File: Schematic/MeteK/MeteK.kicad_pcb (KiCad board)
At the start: 2 copper layers, 1 part, among them U2 LM7805_TO220

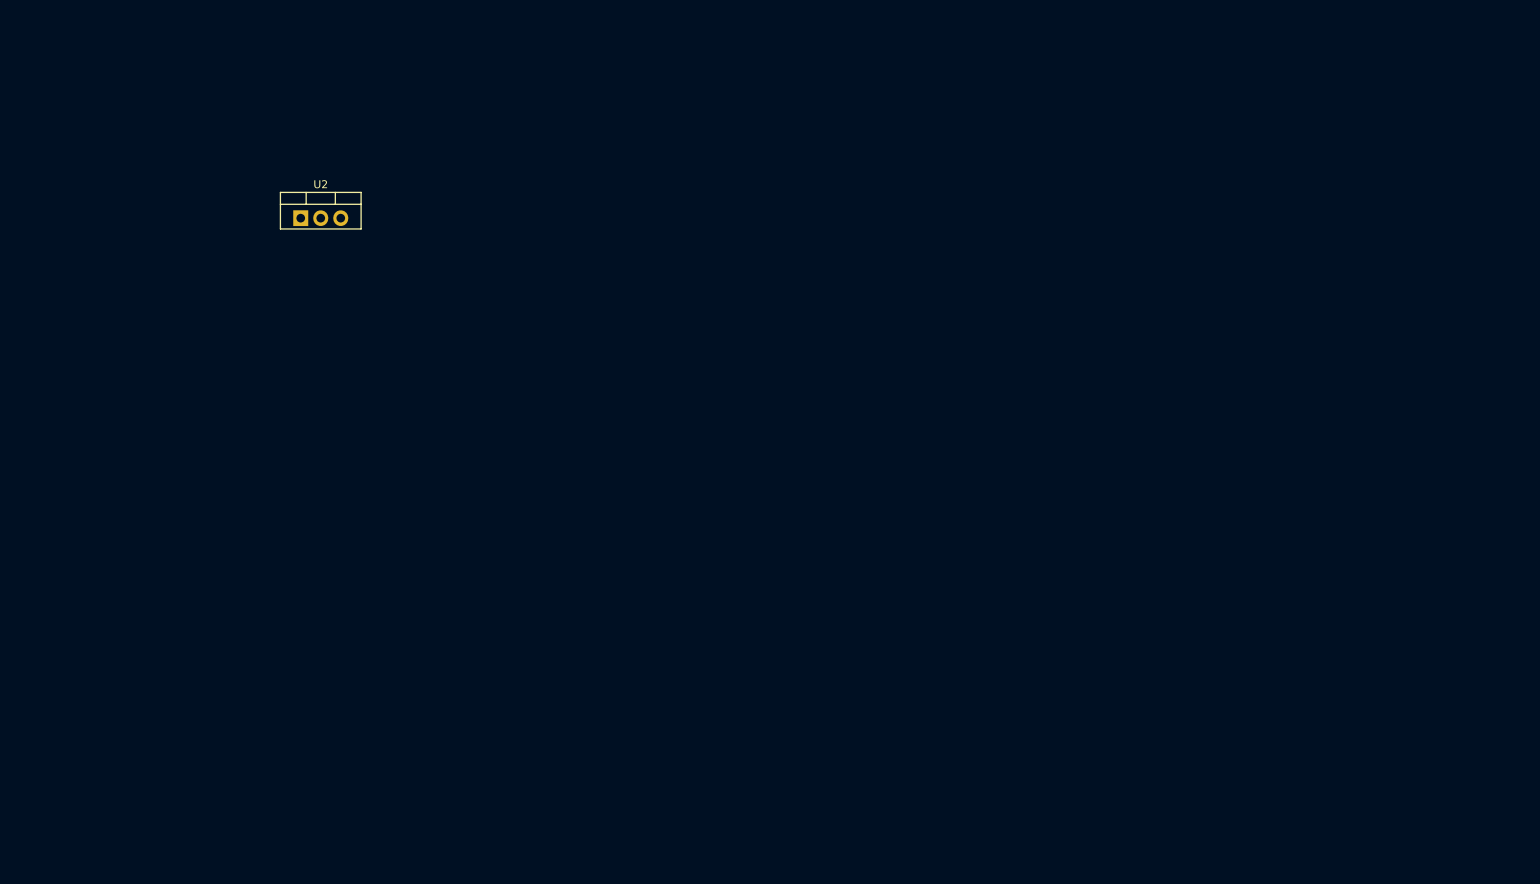
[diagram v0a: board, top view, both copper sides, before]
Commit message: Gate driver fixes. Initial KiCad schematic and PCB design trials. Updates on components.
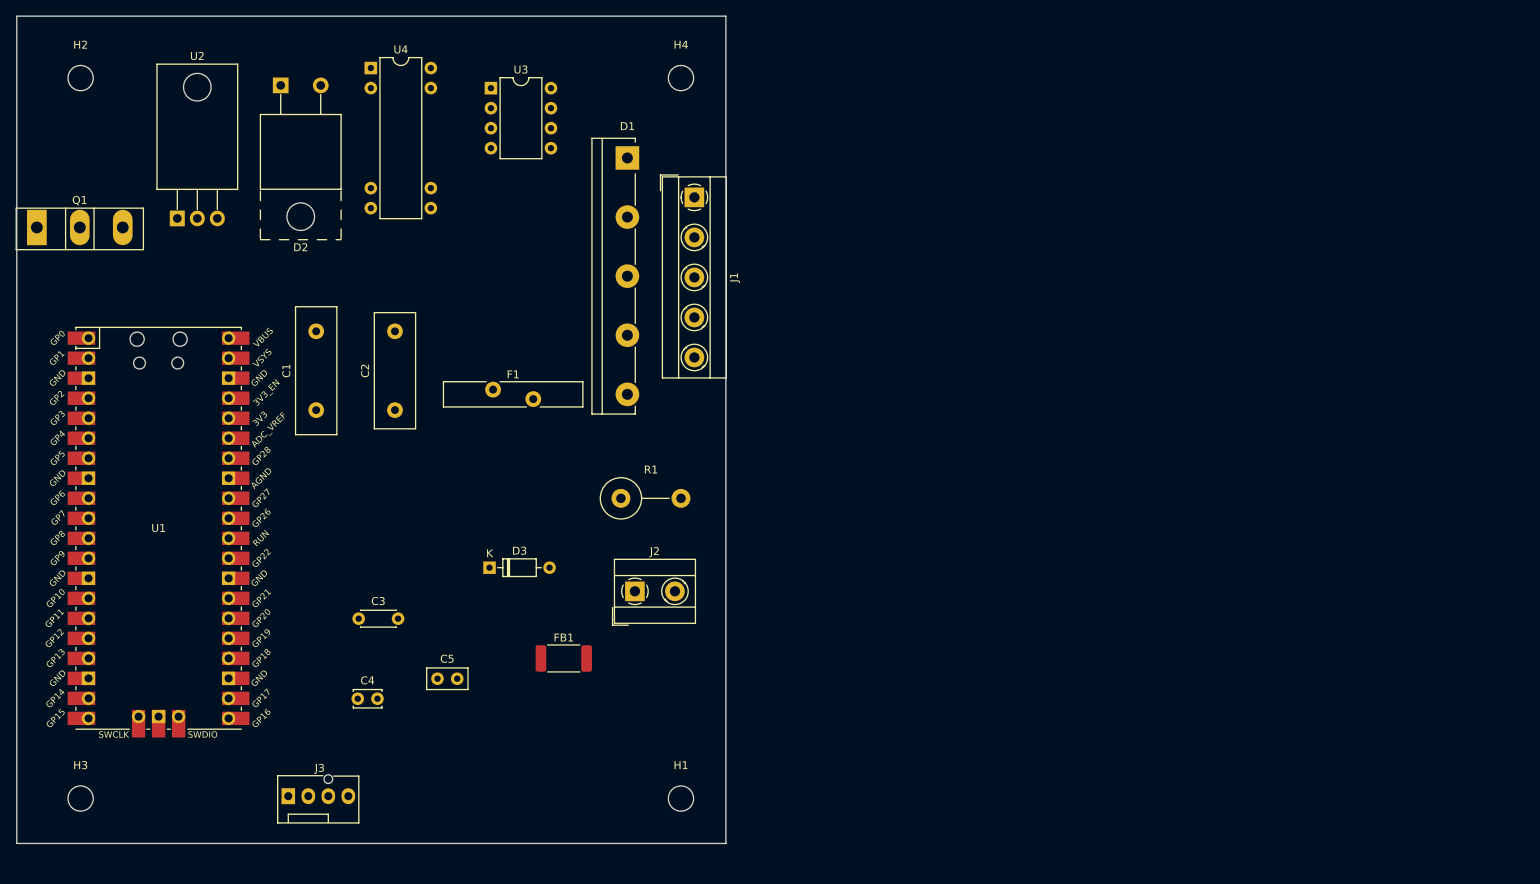
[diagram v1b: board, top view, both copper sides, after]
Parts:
- added C1: 100u, Capacitor_THT:C_Disc_D16.0mm_W5.0mm_P10.00mm, F.Cu at (68.0, 65.0)
- added C2: 0.1u, Capacitor_THT:C_Disc_D14.5mm_W5.0mm_P10.00mm, F.Cu at (78.0, 65.0)
- added C3: 0.1u, Capacitor_THT:C_Disc_D4.3mm_W1.9mm_P5.00mm, F.Cu at (73.4, 91.5)
- added C4: 0.33u, Capacitor_THT:C_Disc_D3.4mm_W2.1mm_P2.50mm, F.Cu at (73.3, 101.6)
- added C5: 0.1u, Capacitor_THT:C_Disc_D5.0mm_W2.5mm_P2.50mm, F.Cu at (83.4, 99.1)
- added D1: GUO40-12NO1, Diode_THT:Diode_Bridge_IXYS_GUFP, F.Cu at (107.5, 33.0)
- added D2: DIODE, Package_TO_SOT_THT:TO-220-2_Horizontal_TabUp, F.Cu at (63.5, 23.8)
- added D3: 1N4148, Diode_THT:D_DO-35_SOD27_P7.62mm_Horizontal, F.Cu at (90.0, 85.0)
- added F1: Fuse, Fuse:Fuse_Bourns_MF-RG1100, F.Cu at (90.5, 62.4)
- added FB1: FerriteBead_Small, Inductor_SMD:L_2512_6332Metric, F.Cu at (99.4, 96.5)
- added H1: MountingHole, MountingHole:MountingHole_3.2mm_M3, F.Cu at (114.3, 114.3)
- added H2: MountingHole, MountingHole:MountingHole_3.2mm_M3, F.Cu at (38.1, 22.9)
- added H3: MountingHole, MountingHole:MountingHole_3.2mm_M3, F.Cu at (38.1, 114.3)
- added H4: MountingHole, MountingHole:MountingHole_3.2mm_M3, F.Cu at (114.3, 22.9)
- added J1: Screw_Terminal_01x05, TerminalBlock_MetzConnect:TerminalBlock_MetzConnect_Type101_RT01605HBWC_1x05_P5.08mm_Horizontal, F.Cu at (116.0, 38.0)
- added J2: Screw_Terminal_01x02, TerminalBlock_MetzConnect:TerminalBlock_MetzConnect_Type101_RT01602HBWC_1x02_P5.08mm_Horizontal, F.Cu at (108.5, 88.0)
- added J3: Conn_01x04_Female, Connector:FanPinHeader_1x04_P2.54mm_Vertical, F.Cu at (64.5, 114.0)
- added Q1: IRG4PF50W, Package_TO_SOT_THT:TO-247-3_Vertical, F.Cu at (32.5, 41.8)
- added R1: R, Resistor_THT:R_Axial_DIN0516_L15.5mm_D5.0mm_P7.62mm_Vertical, F.Cu at (106.7, 76.2)
- added U1: Pico, MCU_RaspberryPi_and_Boards:RPi_Pico_SMD_TH, F.Cu at (48.0, 80.0)
- added U3: HCPL-3120, Package_DIP:DIP-8_W7.62mm, F.Cu at (90.2, 24.1)
- added U4: LM358, Package_DIP:DIP-8-16_W7.62mm, F.Cu at (74.9, 21.6)
- U2: footprint Package_TO_SOT_THT:TO-220-3_Vertical -> Package_TO_SOT_THT:TO-220-3_Horizontal_TabDown
- moved U2 15.7 mm to (50.4, 40.7)
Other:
- board outline added: 90 x 105 mm

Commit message: further tests on schematic and pcb layout.
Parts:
- removed FB1: FerriteBead_Small, Inductor_SMD:L_2512_6332Metric
- added C10: 0.33uF, Capacitor_SMD:C_1206_3216Metric, F.Cu at (200.5, 117.1)
- added C11: 0.1uF, Capacitor_SMD:C_1206_3216Metric, F.Cu at (200.5, 114.1)
- added C12: 0.1uF, Capacitor_SMD:C_1206_3216Metric, F.Cu at (193.0, 79.9)
- added C13: 0.01uF, Capacitor_SMD:C_1206_3216Metric, F.Cu at (204.6, 83.7)
- added C6: 470u, Capacitor_THT:CP_Radial_D35.0mm_P10.00mm_SnapIn, B.Cu at (134.8, 89.8)
- added C7: 470u, Capacitor_THT:CP_Radial_D35.0mm_P10.00mm_SnapIn, B.Cu at (137.8, 54.2)
- added C8: 0.01uF, Capacitor_SMD:C_1206_3216Metric, F.Cu at (151.2, 111.5)
- added C9: 0.1uF, Capacitor_SMD:C_1206_3216Metric, F.Cu at (147.4, 111.5)
- added J4: Conn_01x03_Female, Connector_PinHeader_2.54mm:PinHeader_1x03_P2.54mm_Vertical, F.Cu at (198.2, 80.5)
- added L1: 27n, Inductor_SMD:L_1206_3216Metric, F.Cu at (175.2, 80.2)
- added R2: 220R, Resistor_SMD:R_0805_2012Metric, F.Cu at (156.0, 101.0)
- added R3: 220R, Resistor_SMD:R_0805_2012Metric, F.Cu at (156.0, 97.5)
- added R4: 22R, Resistor_SMD:R_0805_2012Metric, F.Cu at (162.2, 101.0)
- added R5: 22kR, Resistor_SMD:R_0805_2012Metric, F.Cu at (203.4, 77.1)
- added R6: 39kR, Resistor_SMD:R_0805_2012Metric, F.Cu at (206.5, 77.1)
- added R7: 440, Resistor_SMD:R_0805_2012Metric, F.Cu at (189.9, 84.5)
- added U5: L78L12_SOT89, Package_TO_SOT_SMD:SOT-89-3, F.Cu at (207.2, 115.6)
- added U6: LM358, Package_DIP:DIP-8_W7.62mm, F.Cu at (209.4, 76.1)
- C1: value 100u -> 1uF; footprint Capacitor_THT:C_Disc_D16.0mm_W5.0mm_P10.00mm -> Capacitor_SMD:C_1206_3216Metric
- C2: value 0.1u -> 0.1uF; footprint Capacitor_THT:C_Disc_D14.5mm_W5.0mm_P10.00mm -> Capacitor_SMD:C_1206_3216Metric
- C3: value 0.1u -> 0.33uF; footprint Capacitor_THT:C_Disc_D4.3mm_W1.9mm_P5.00mm -> Capacitor_SMD:C_1206_3216Metric
- C4: value 0.33u -> 0.33uF; footprint Capacitor_THT:C_Disc_D3.4mm_W2.1mm_P2.50mm -> Capacitor_SMD:C_1206_3216Metric
- C5: value 0.1u -> 0.1uF; footprint Capacitor_THT:C_Disc_D5.0mm_W2.5mm_P2.50mm -> Capacitor_SMD:C_1206_3216Metric
- D2: footprint Package_TO_SOT_THT:TO-220-2_Horizontal_TabUp -> Package_TO_SOT_THT:TO-220-2_Vertical
- D3: footprint Diode_THT:D_DO-35_SOD27_P7.62mm_Horizontal -> Diode_SMD:D_SMB
- F1: footprint Fuse:Fuse_Bourns_MF-RG1100 -> Fuse:Fuseholder_Clip-5x20mm_Bel_FC-203-22_Lateral_P17.80x5.00mm_D1.17mm_Horizontal
- H1, H2, H3, H4: footprint MountingHole:MountingHole_3.2mm_M3 -> MountingHole:MountingHole_3.2mm_M3_Pad
- J3: value Conn_01x04_Female -> Conn_01x02_Female; footprint Connector:FanPinHeader_1x04_P2.54mm_Vertical -> Connector_PinHeader_2.54mm:PinHeader_1x02_P2.54mm_Vertical
- R1: value R -> 220; footprint Resistor_THT:R_Axial_DIN0516_L15.5mm_D5.0mm_P7.62mm_Vertical -> Resistor_SMD:R_0603_1608Metric
- U2: value LM7805_TO220 -> L78L33_SOT89; footprint Package_TO_SOT_THT:TO-220-3_Horizontal_TabDown -> Package_TO_SOT_SMD:SOT-89-3
- U4: value LM358 -> L78L05_SOT89; footprint Package_DIP:DIP-8-16_W7.62mm -> Package_TO_SOT_SMD:SOT-89-3
- moved Q1 151.2 mm to (181.5, 68.0), turned to 90 degrees
- moved U1 145.7 mm to (192.5, 99.0), turned to 90 degrees
- moved J3 130.3 mm to (194.7, 116.6), turned to 180 degrees
- moved H2 128.7 mm to (122.5, 120.0)
- moved U4 125.1 mm to (187.1, 76.9), turned to 180 degrees
- moved C3 120.8 mm to (193.1, 75.4)
- moved U2 119.9 mm to (163.5, 80.4), turned to 180 degrees
- moved U3 115.8 mm to (163.5, 113.8), turned to 180 degrees
- moved H3 114.1 mm to (122.5, 37.5)
- moved C1 114.0 mm to (180.3, 84.6), turned to 0 degrees
- moved D2 106.6 mm to (162.8, 62.5), turned to -90 degrees
- moved F1 105.0 mm to (193.7, 43.1), turned to 180 degrees
- moved H4 104.2 mm to (217.5, 37.5)
- moved H1 103.4 mm to (217.5, 120.0)
- moved C2 101.7 mm to (178.5, 80.3)
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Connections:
- net +5VA renamed +3.3VA
- C3 pad 1: +5V -> VCC
- C5 pad 1: +5V -> +3.3V
- D1 pad 1: unconnected-(D1-Pad1) -> Net-(D1-Pad1)
- D1 pad 2: unconnected-(D1-Pad2) -> AC_c
- D1 pad 3: unconnected-(D1-Pad3) -> AC_b
- D1 pad 4: unconnected-(D1-Pad4) -> AC_a
- D1 pad 5: unconnected-(D1-Pad5) -> REC_-
- D2 pad 1: unconnected-(D2-Pad1) -> A-
- D2 pad 2: unconnected-(D2-Pad2) -> A+
- D3 pad 1: unconnected-(D3-Pad1) -> Net-(D3-Pad1)
- D3 pad 2: unconnected-(D3-Pad2) -> Net-(D3-Pad2)
- F1 pad 1: unconnected-(F1-Pad1) -> Net-(D1-Pad1)
- F1 pad 2: unconnected-(F1-Pad2) -> A+
- J1 pad 1: unconnected-(J1-Pad1) -> AC_c
- J1 pad 2: unconnected-(J1-Pad2) -> AC_b
- J1 pad 3: unconnected-(J1-Pad3) -> AC_a
- J1 pad 4: unconnected-(J1-Pad4) -> VCC
- J1 pad 5: unconnected-(J1-Pad5) -> GND
- J2 pad 1: unconnected-(J2-Pad1) -> A-
- J2 pad 2: unconnected-(J2-Pad2) -> A+
- J3 pad 1: unconnected-(J3-Pad1) -> GND
- J3 pad 2: unconnected-(J3-Pad2) -> +12V
- Q1 pad 1: unconnected-(Q1-Pad1) -> GATE
- Q1 pad 2: unconnected-(Q1-Pad2) -> A-
- Q1 pad 3: unconnected-(Q1-Pad3) -> REC_-
- R1 pad 1: unconnected-(R1-Pad1) -> PWM
- R1 pad 2: unconnected-(R1-Pad2) -> Net-(R1-Pad2)
- U1 pad 1: unconnected-(U1-Pad1) -> PWM
- U1 pad 19: PWM -> unconnected-(U1-Pad19)
- U1 pad 31: unconnected-(U1-Pad31) -> Net-(U1-Pad31)
- U1 pad 39: +5V -> +3.3V
- U1 pad 40: +5V -> unconnected-(U1-Pad40)
- U2 pad 1: VCC -> +3.3V
- U2 pad 3: +5V -> VCC
- U3 pad 2: unconnected-(U3-Pad2) -> Net-(R1-Pad2)
- U3 pad 3: unconnected-(U3-Pad3) -> GND
- U3 pad 5: unconnected-(U3-Pad5) -> REC_-
- U3 pad 6: unconnected-(U3-Pad6) -> Net-(D3-Pad1)
- U3 pad 7: unconnected-(U3-Pad7) -> Net-(D3-Pad1)
- U3 pad 8: unconnected-(U3-Pad8) -> VCC
- U4 pad 1: unconnected-(U4-Pad1) -> +5V
- U4 pad 2: unconnected-(U4-Pad2) -> GND
- U4 pad 3: unconnected-(U4-Pad3) -> VCC
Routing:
- net VCC: track 0.00 -> 210.3 mm
- net GND: track 0.00 -> 84.0 mm, vias 0 -> 26
- net GATE: track 0.00 -> 59.4 mm
- net REC_-: track 0.00 -> 53.0 mm
- net +3.3V: track 0.00 -> 22.7 mm
- net Net-(D3-Pad1): track 0.00 -> 21.1 mm
- net C_ADC: track 0.00 -> 20.0 mm
- net +12V: track 0.00 -> 13.4 mm
- net +3.3VA: track 0.00 -> 12.7 mm
- net +5V: track 0.00 -> 10.3 mm
- net Net-(D3-Pad2): track 0.00 -> 8.11 mm
- net Net-(U1-Pad31): track 0.00 -> 6.54 mm
- net Net-(R5-Pad2): track 0.00 -> 6.04 mm
- net Net-(R1-Pad2): track 0.00 -> 5.91 mm
- net CSENSE: track 0.00 -> 5.62 mm
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- added copper zone on B.Cu, net A+
- added copper zone on F.Cu, net A+
- added copper zone on B.Cu, net A-
- added copper zone on F.Cu, net A-
- added copper zone on F.Cu, net AC_a
- added copper zone on F.Cu, net AC_b
- added copper zone on F.Cu, net AC_c
- added copper zone on B.Cu, net GND
- added copper zone on F.Cu, net GND
- added copper zone on F.Cu, net Net-(D1-Pad1)
- added copper zone on B.Cu, net REC_-
- added copper zone on F.Cu, net REC_-
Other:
- board outline removed
